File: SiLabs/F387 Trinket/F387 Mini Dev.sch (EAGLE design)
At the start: 17 parts, among them J1 1X7, J2 1X7, J3 1X1, SW1 SPST.B3U-1000P(M)-B, U1 C8051F387, U2 SP0503BAHTG

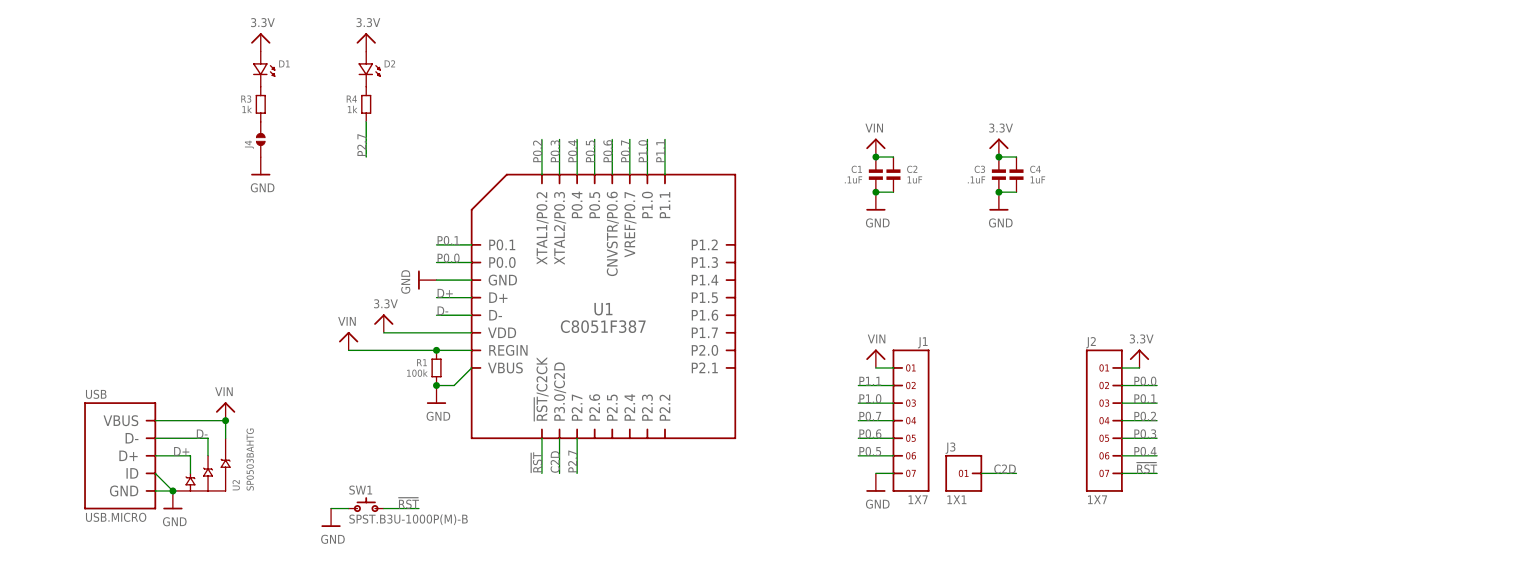
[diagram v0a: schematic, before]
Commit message: Redid Trinket clone to add FTDI header capabilities Replaced USB ESD protection IC with tinier variant. All passives are now 0402 sized (oh boy...) Power domains should be fixed as well
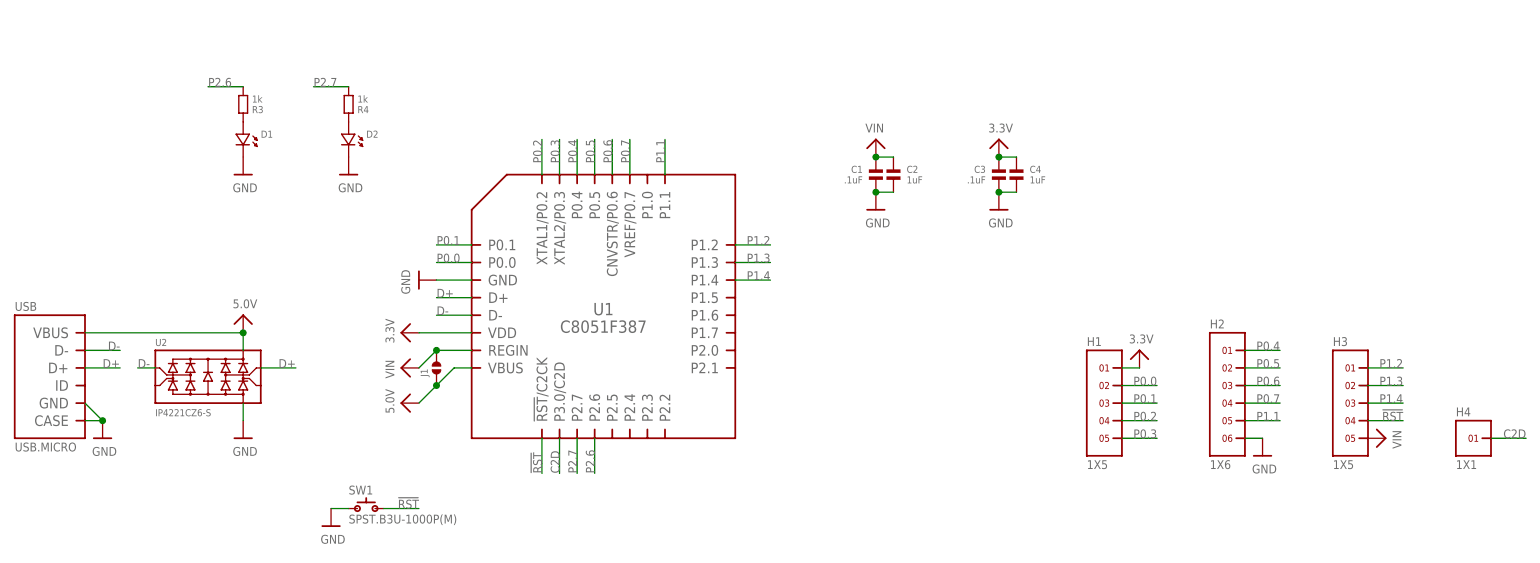
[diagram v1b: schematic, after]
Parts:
- removed J2: 1X7, headers(.1in):1X7
- removed J3: 1X1, headers(.1in):1X1
- removed J4: (no value), solderjumper:SOLDERJUMPER.2.MED.PASTE
- removed R1: 100k, standardparts:RESISTOR.0603
- added H1, H3: 1X5, headers(.1in):1X5
- added H2: 1X6, headers(.1in):1X6
- added H4: 1X1, headers(2mm):1X1
- C1, C2, C3, C4: device standardparts:CAPACITOR.0603 -> standardparts:CAPACITOR.0402
- D1, D2: device standardparts:LED.0603 -> standardparts:LED.0402
- J1: value 1X7 -> (none); device headers(.1in):1X7 -> solderjumper:SOLDERJUMPER.2.SML
- R3, R4: device standardparts:RESISTOR.0603 -> standardparts:RESISTOR.0402
- SW1: value SPST.B3U-1000P(M)-B -> SPST.B3U-1000P(M); device omron:SPST.B3U-1000P(M)-B -> omron:SPST.B3U-1000P(M)
- U2: value SP0503BAHTG -> IP4221CZ6-S; device littlefuse:SP0503BAHTG -> nxp:IP4221CZ6-S
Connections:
- removed net N$3: D2.2, R4.1
- removed net P1.0: J1.3, U1.P1.0
- new net 5.0V: J1.1, U1.VBUS, U2.5, USB.VBUS
- new net P1.2: H3.1, U1.P1.2
- new net P1.3: H3.2, U1.P1.3
- new net P1.4: H3.3, U1.P1.4
- new net P2.6: R3.2, U1.P2.6
- net !RST: now also H3.4; no longer J2.7
- net 3.3V: now also H1.1; no longer D1.1, D2.1, J2.1
- net C2D: now also H4.1; no longer J3.1
- net D+: now also U2.3; no longer U2.A
- net D-: now also U2.1; no longer U2.B
- net GND: now also D1.2, D2.2, H2.6, U2.2, USB.CASE; no longer J1.7, J4.1, R1.2, U1.VBUS, U2.GND, USB.ID
- net N$1: now also D1.1; no longer D1.2
- net N$2: now also D2.1, R4.1; no longer J4.2, R3.2
- net P0.0: now also H1.2; no longer J2.2
- net P0.1: now also H1.3; no longer J2.3
- net P0.2: now also H1.4; no longer J2.4
- net P0.3: now also H1.5; no longer J2.5
- net P0.4: now also H2.1; no longer J2.6
- net P0.5: now also H2.2; no longer J1.6
- net P0.6: now also H2.3; no longer J1.5
- net P0.7: now also H2.4; no longer J1.4
- net P1.1: now also H2.5; no longer J1.2
- net VIN: now also H3.5, J1.2; no longer J1.1, R1.1, U2.C, USB.VBUS
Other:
- moved on the sheet: D1, D2, R3, R4
